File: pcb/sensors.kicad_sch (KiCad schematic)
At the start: 21 parts, among them J3 Conn_01x04, J4 Conn_01x04, J5 6P4C, J6 Conn_02x05_Odd_Even, U4 SN65HVD3082EDR, U5 TXS0108EPW, U6 BME280, U7 SGP41

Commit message: feat: finalized main system schematic
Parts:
- J3, J4: now in the parts list
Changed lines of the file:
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@@
 		(unit 1)
 		(exclude_from_sim no)
-		(in_bom no)
+		(in_bom yes)
 		(on_board yes)
 		(dnp no)
@@
 		(unit 1)
 		(exclude_from_sim no)
-		(in_bom no)
-		(on_board yes)
-		(dnp no)
+		(in_bom yes)
+		(on_board yes)
+		(dnp no)

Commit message: chore: page documentation
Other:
- title: Banshee Microcontroller + Supporting Systems -> Banshee Sensor Collection
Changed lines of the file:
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@@
 	(paper "A4")
 	(title_block
-		(title "Banshee Microcontroller + Supporting Systems")
-		(date "2026-02-05")
+		(title "Banshee Sensor Collection")
+		(date "2026-02-18")
 		(rev "1")
 		(company "Ivan Leonard O Aparte <ivanleonard.aparte@cit.edu>")
+		(comment 1 "STEM 12 - Altruism | S.Y. 2025-2026")
 	)
 	(text "pp.32, ch.6.1 of the BME280 datasheet\nstates that CSB must be connected to\nVDD_{IO} in order for the I^{2}C\ninterface to be selected"

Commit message: feat: radio schematic
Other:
- title: Banshee Sensor Collection -> Banshee Power Delivery System
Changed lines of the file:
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@@
 	(paper "A4")
 	(title_block
-		(title "Banshee Sensor Collection")
-		(date "2026-02-18")
+		(title "Banshee Power Delivery System")
+		(date "2026-02-26")
 		(rev "1")
 		(company "Ivan Leonard O Aparte <ivanleonard.aparte@cit.edu>")

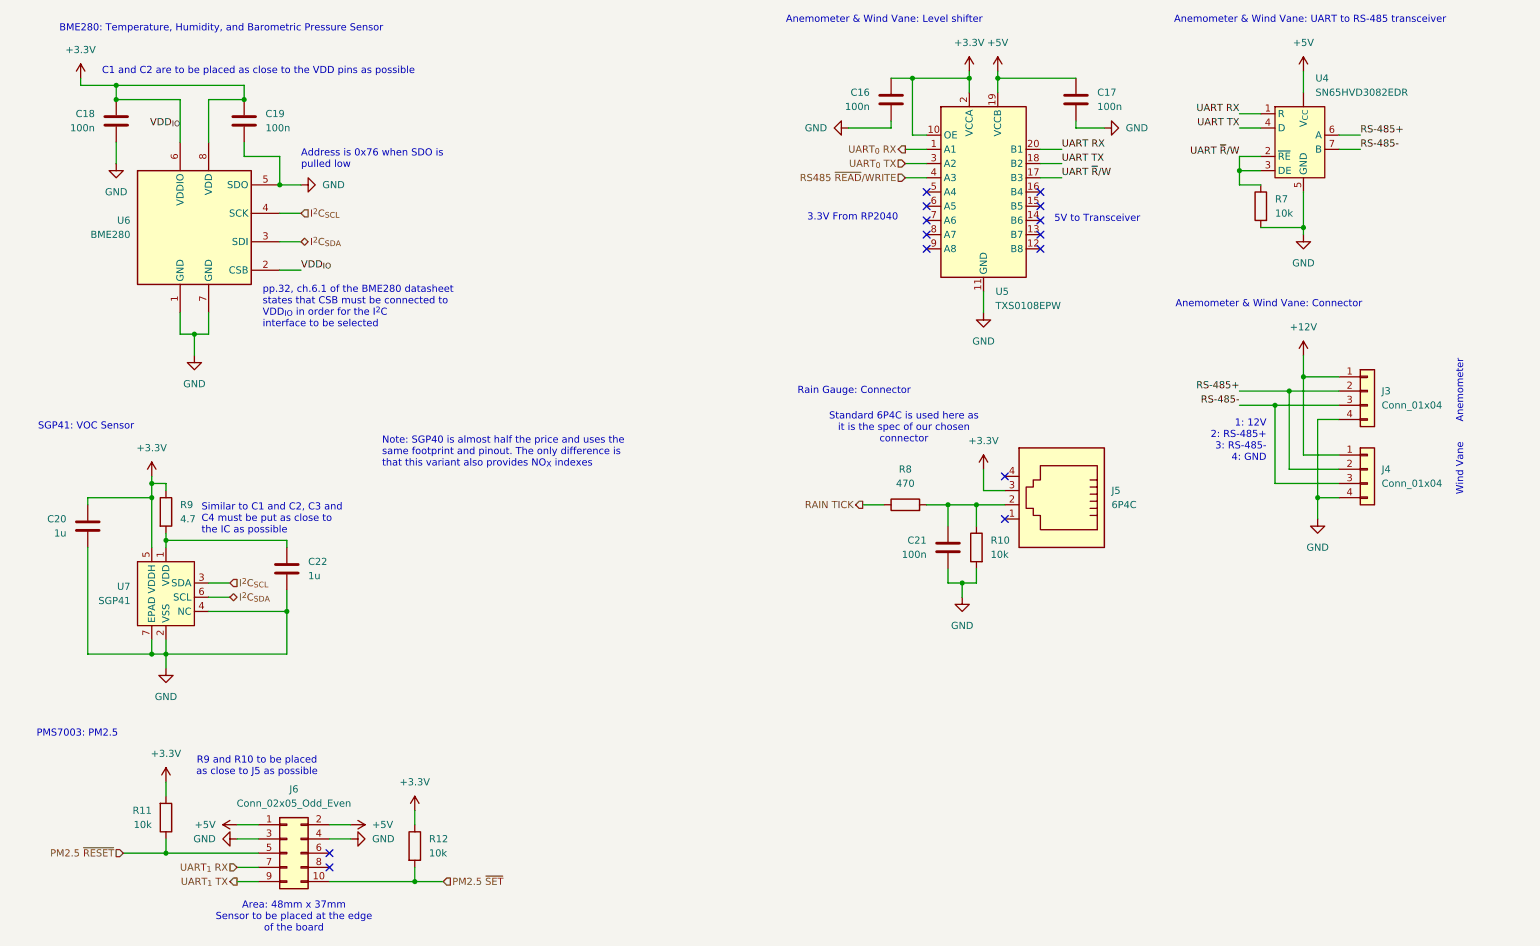
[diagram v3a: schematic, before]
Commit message: feat: revised 3.3v power rail, added power switch
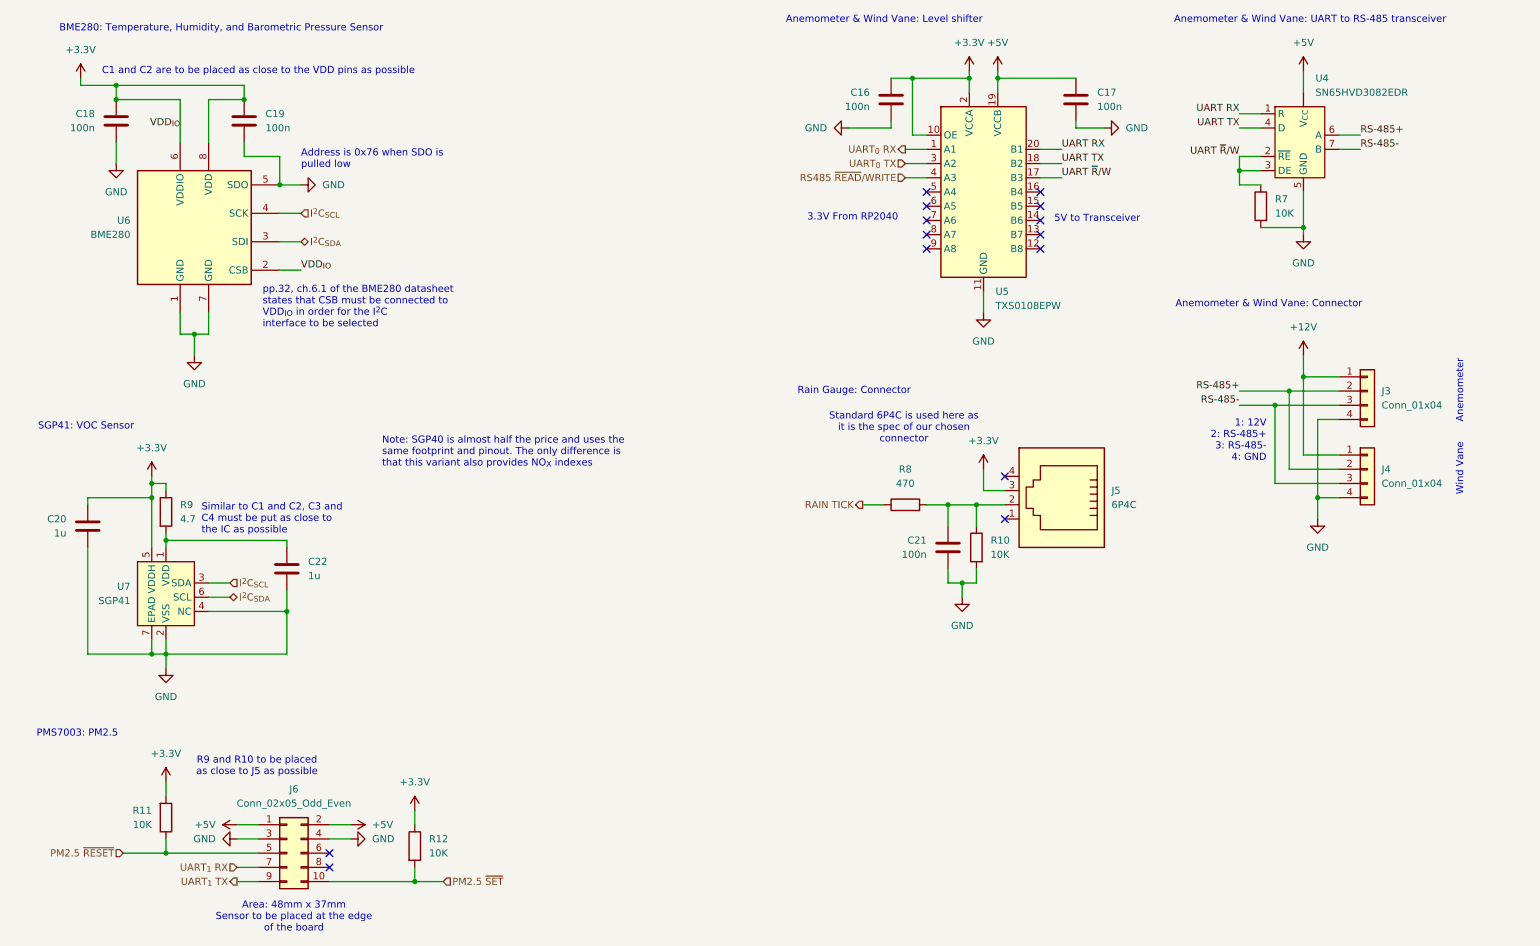
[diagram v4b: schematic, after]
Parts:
- R10, R11, R12, R7: value 10k -> 10K
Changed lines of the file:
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@@
 			)
 		)
-		(property "Value" "10k"
+		(property "Value" "10K"
 			(at 41.91 160.0199 0)
 			(effects
@@
 			)
 		)
-		(property "Value" "10k"
+		(property "Value" "10K"
 			(at 242.57 50.7999 0)
 			(effects
@@
 			)
 		)
-		(property "Value" "10k"
+		(property "Value" "10K"
 			(at 91.44 165.0999 0)
 			(effects
@@
 			)
 		)
-		(property "Value" "10k"
+		(property "Value" "10K"
 			(at 191.77 111.7599 0)
 			(effects

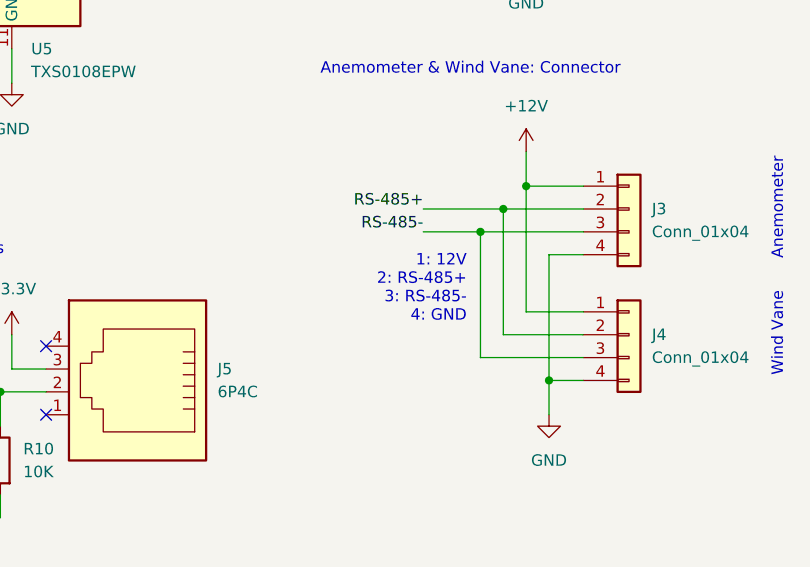
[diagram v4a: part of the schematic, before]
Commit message: feat: added documentation, updated page information
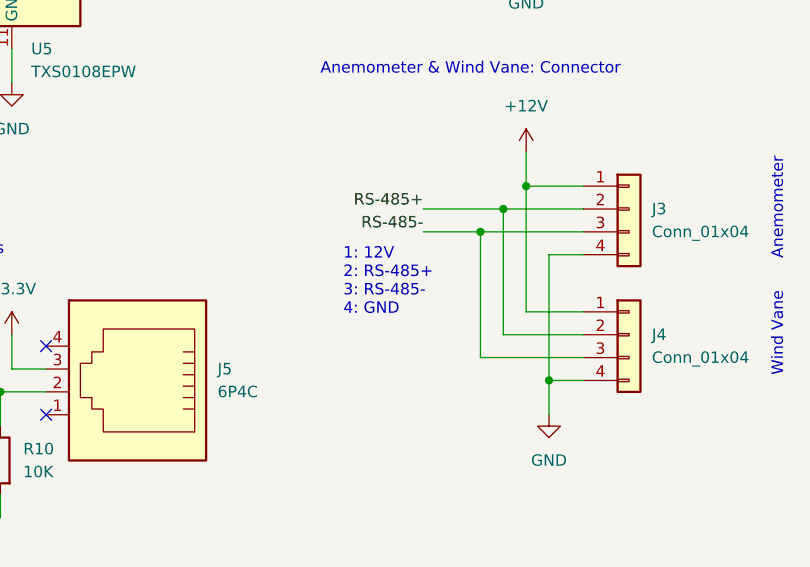
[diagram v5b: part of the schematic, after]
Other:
- title: Banshee Power Delivery System -> Banshee Sensor Collection
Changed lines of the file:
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@@
 	(paper "A4")
 	(title_block
-		(title "Banshee Power Delivery System")
+		(title "Banshee Sensor Collection")
 		(date "2026-02-26")
 		(rev "1")
@@
 			(font
 				(size 1.27 1.27)
+				(color 194 0 0 1)
 			)
 			(justify left)
@@
 			(font
 				(size 1.27 1.27)
+				(color 194 0 0 1)
 			)
 		)
@@
 			(font
 				(size 1.27 1.27)
+				(color 194 0 0 1)
 			)
 			(href "https://jlcpcb.com/api/file/downloadByFileSystemAccessId/8589835483552378880")
@@
 	(text "1: 12V\n2: RS-485+\n3: RS-485-\n4: GND"
 		(exclude_from_sim no)
-		(at 241.046 91.44 0)
+		(at 227.33 90.678 0)
 		(effects
 			(font
 				(size 1.27 1.27)
+				(color 194 0 0 1)
 			)
-			(justify right)
+			(justify left)
 		)
 	)
@@
 			(font
 				(size 1.27 1.27)
+				(color 194 0 0 1)
 			)
 		)

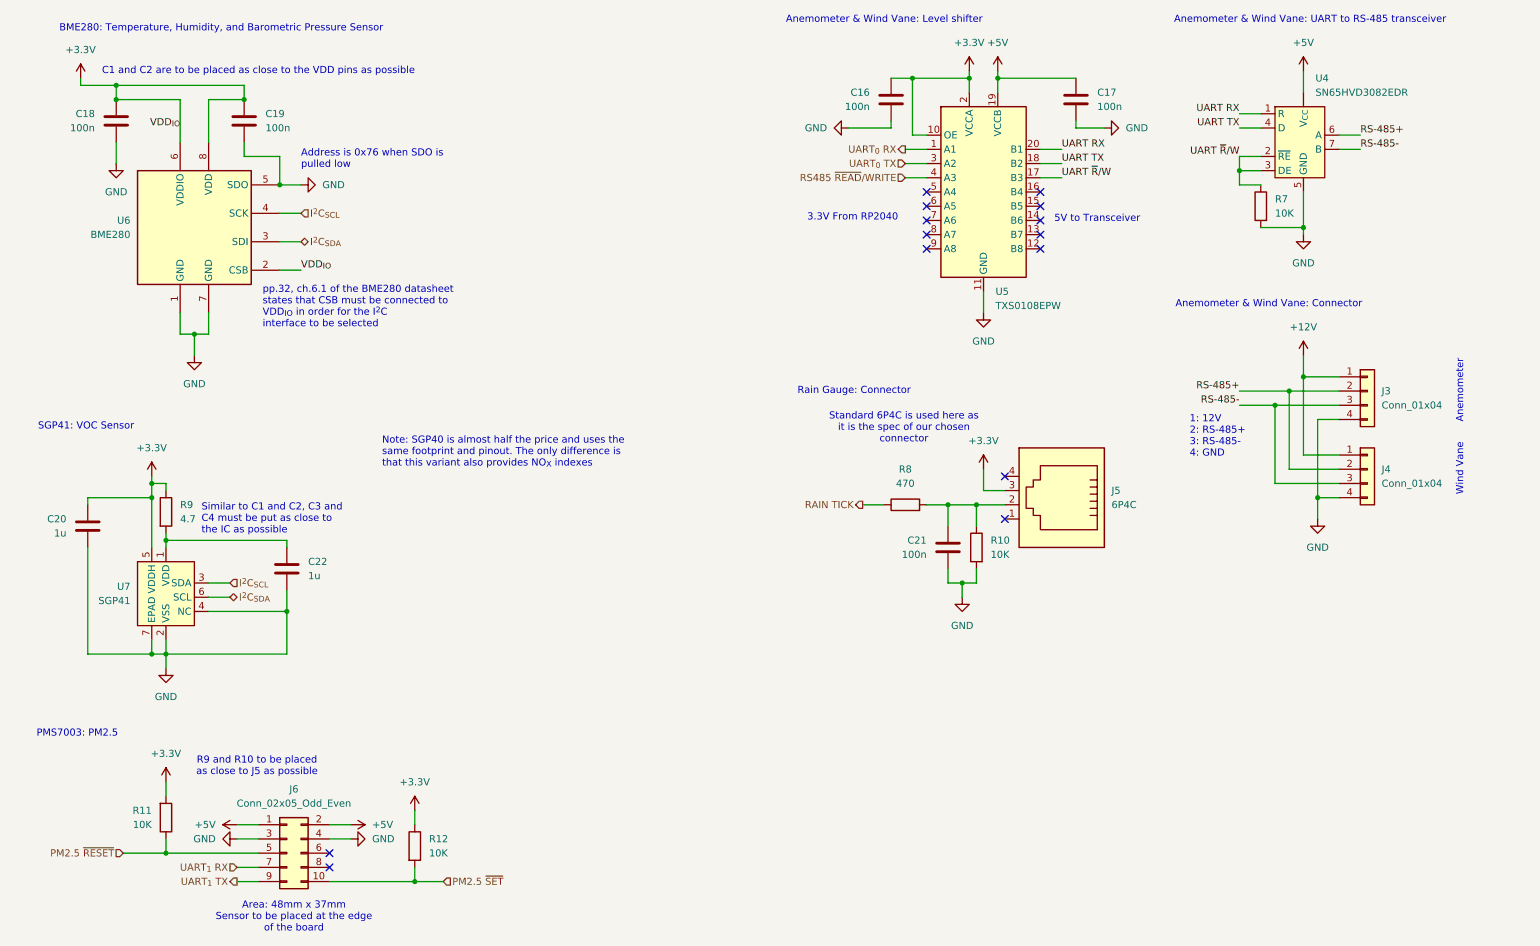
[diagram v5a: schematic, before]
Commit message: chore: re-annotated schematic symbols
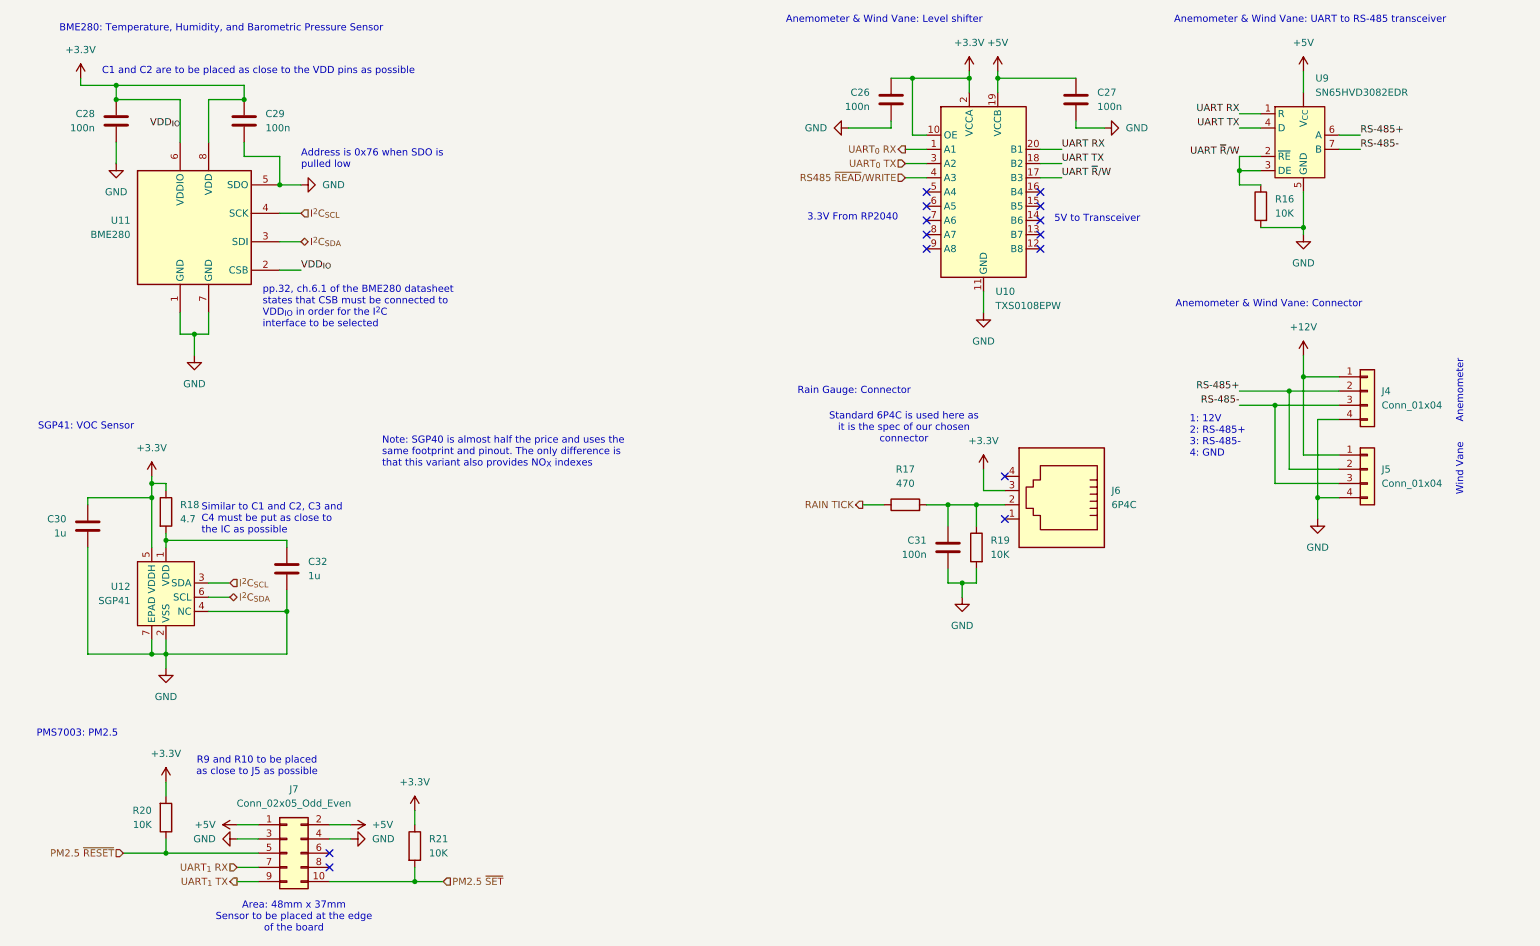
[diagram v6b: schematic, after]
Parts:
- renumbered C16 to C26, C17 to C27, C18 to C28, C19 to C29, C20 to C30, C21 to C31, C22 to C32, J3 to J4, J4 to J5, J5 to J6, J6 to J7, R7 to R16, R8 to R17, R9 to R18, R10 to R19, R11 to R20, R12 to R21, U5 to U10, U6 to U11, U7 to U12, U4 to U9
